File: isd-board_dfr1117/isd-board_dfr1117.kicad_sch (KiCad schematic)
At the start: 50 parts, among them J1 BATT, J10 Conn_01x13, J2 Conn_01x08, J3 Conn_01x02_Pin, J4 Conn_01x08, J5 Conn_01x04, J6 Conn_01x04, J7 Conn_01x05, J8 USB_C_Receptacle_PowerOnly_6P, J9 Conn_01x02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

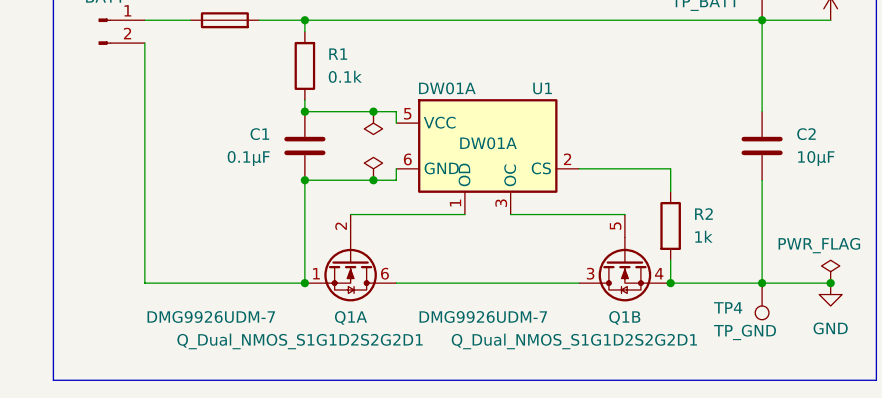
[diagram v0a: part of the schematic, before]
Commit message: update: battery protection circuit (compact placement)
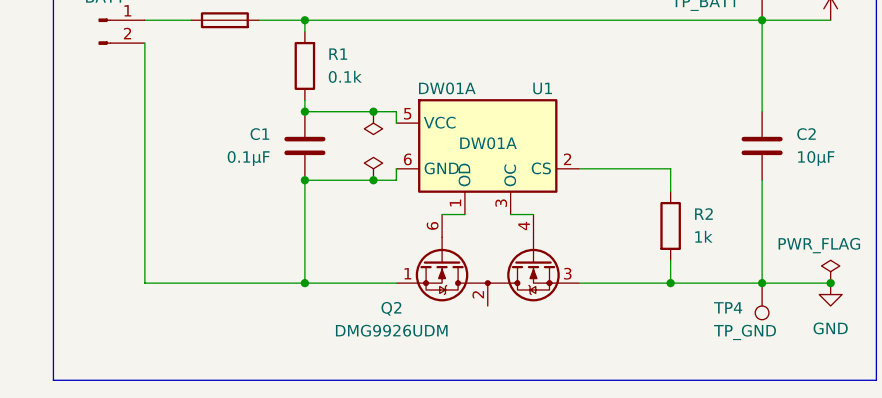
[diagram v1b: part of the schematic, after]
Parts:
- removed Q1: Q_Dual_NMOS_S1G1D2S2G2D1, Package_TO_SOT_SMD:SOT-23-6_Handsoldering, symbol Transistor_FET:Q_Dual_NMOS_S1G1D2S2G2D1
- added Q2: DMG9926UDM, Package_TO_SOT_SMD:SOT-23-6, symbol Transistor_FET:DMG9926UDM
- TP2, TP3, TP4, TP5, TP6, TP7: footprint TestPoint:TestPoint_Pad_D2.5mm -> TestPoint:TestPoint_Pad_D1.0mm
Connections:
- net GND: now also Q2.3 (S2)
- net at U1.1 (OD): now also Q2.6 (G1)
- net at U1.3 (OC): now also Q2.4 (G2)
- net at C1.2, J1.2 (Pin_2), U1.6 (GND): now also Q2.1 (D1)
- new net: Q2.2 (S1/D2), Q2.5 (S1/D2)
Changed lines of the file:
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@@
 	)
 	(junction
-		(at 46.99 181.61)
+		(at 87.63 181.61)
 		(diameter 0)
 		(color 0 0 0 0)
@@
 	)
 	(junction
-		(at 87.63 181.61)
-		(diameter 0)
-		(color 0 0 0 0)
-	)
-	(junction
 		(at 57.15 101.6)
 		(diameter 0)
@@
 	)
 	(junction
+		(at 46.99 181.61)
+		(diameter 0)
+		(color 0 0 0 0)
+	)
+	(junction
 		(at 54.61 162.56)
 		(diameter 0)
@@
 	(wire
 		(pts
-			(xy 57.15 181.61) (xy 77.47 181.61)
+			(xy 242.57 77.47) (xy 245.11 77.47)
 		)
 		(stroke
@@
 	(wire
 		(pts
-			(xy 242.57 77.47) (xy 245.11 77.47)
+			(xy 97.79 152.4) (xy 97.79 162.56)
 		)
 		(stroke
@@
 	(wire
 		(pts
-			(xy 97.79 152.4) (xy 97.79 162.56)
+			(xy 57.15 101.6) (xy 57.15 102.87)
 		)
 		(stroke
@@
 	(wire
 		(pts
-			(xy 57.15 101.6) (xy 57.15 102.87)
+			(xy 189.23 156.21) (xy 199.39 156.21)
 		)
 		(stroke
@@
 	(wire
 		(pts
-			(xy 189.23 156.21) (xy 199.39 156.21)
+			(xy 29.21 154.94) (xy 29.21 181.61)
 		)
 		(stroke
@@
 	(wire
 		(pts
-			(xy 29.21 154.94) (xy 29.21 181.61)
+			(xy 46.99 170.18) (xy 46.99 181.61)
 		)
 		(stroke
@@
 	(wire
 		(pts
-			(xy 46.99 170.18) (xy 46.99 181.61)
+			(xy 77.47 181.61) (xy 87.63 181.61)
 		)
 		(stroke
@@
 	(wire
 		(pts
+			(xy 62.23 173.99) (xy 64.77 173.99)
+		)
+		(stroke
+			(width 0)
+			(type default)
+		)
+	)
+	(wire
+		(pts
 			(xy 30.48 91.44) (xy 30.48 92.71)
 		)
@@
 	(wire
 		(pts
-			(xy 69.85 173.99) (xy 82.55 173.99)
+			(xy 129.54 181.61) (xy 133.35 181.61)
 		)
 		(stroke
@@
 	(wire
 		(pts
-			(xy 129.54 181.61) (xy 133.35 181.61)
+			(xy 167.64 168.91) (xy 162.56 168.91)
 		)
 		(stroke
@@
 	(wire
 		(pts
-			(xy 167.64 168.91) (xy 162.56 168.91)
+			(xy 46.99 181.61) (xy 57.15 181.61)
 		)
 		(stroke
@@
 	(wire
 		(pts
+			(xy 69.85 173.99) (xy 72.39 173.99)
+		)
+		(stroke
+			(width 0)
+			(type default)
+		)
+	)
+	(wire
+		(pts
 			(xy 29.21 152.4) (xy 34.29 152.4)
 		)
@@
 	(wire
 		(pts
-			(xy 52.07 173.99) (xy 64.77 173.99)
-		)
-		(stroke
-			(width 0)
-			(type default)
-		)
-	)
-	(wire
-		(pts
 			(xy 71.12 120.65) (xy 77.47 120.65)
 		)
@@
 			)
 		)
-		(property "Footprint" "TestPoint:TestPoint_Pad_D2.5mm"
+		(property "Footprint" "TestPoint:TestPoint_Pad_D1.0mm"
 			(at 160.02 161.29 0)
 			(effects
@@
 			)
 		)
-		(property "Footprint" "TestPoint:TestPoint_Pad_D2.5mm"
+		(property "Footprint" "TestPoint:TestPoint_Pad_D1.0mm"
 			(at 220.98 120.65 0)
 			(effects
@@
 			)
 		)
-		(property "Footprint" "TestPoint:TestPoint_Pad_D2.5mm"
+		(property "Footprint" "TestPoint:TestPoint_Pad_D1.0mm"
 			(at 92.71 181.61 0)
 			(effects
@@
 			)
 		)
-		(property "Footprint" "TestPoint:TestPoint_Pad_D2.5mm"
+		(property "Footprint" "TestPoint:TestPoint_Pad_D1.0mm"
 			(at 80.01 91.44 0)
 			(effects
@@
 	)
 	(symbol
-		(lib_id "Transistor_FET:Q_Dual_NMOS_S1G1D2S2G2D1")
-		(at 52.07 179.07 270)
-		(unit 1)
-		(exclude_from_sim no)
-		(in_bom yes)
-		(on_board yes)
-		(dnp no)
-		(property "Reference" "Q1"
-			(at 52.07 185.42 90)
-			(effects
-				(font
-					(size 1.27 1.27)
-				)
-			)
-		)
-		(property "Value" "Q_Dual_NMOS_S1G1D2S2G2D1"
-			(at 46.482 187.96 90)
-			(effects
-				(font
-					(size 1.27 1.27)
-				)
-			)
-		)
-		(property "Footprint" "Package_TO_SOT_SMD:SOT-23-6_Handsoldering"
-			(at 52.07 184.15 0)
-			(effects
-				(font
-					(size 1.27 1.27)
-				)
-				(hide yes)
-			)
-		)
-		(property "Datasheet" "https://www.mouser.fi/datasheet/3/175/1/ds31770.pdf"
-			(at 52.07 184.15 0)
-			(effects
-				(font
-					(size 1.27 1.27)
-				)
-				(hide yes)
-			)
-		)
-		(property "Description" "Dual NMOS transistor, 6 pin package"
-			(at 52.07 179.07 0)
-			(effects
-				(font
-					(size 1.27 1.27)
-				)
-				(hide yes)
-			)
-		)
-		(property "MPN" "DMG9926UDM-7"
-			(at 36.576 185.42 90)
-			(effects
-				(font
-					(size 1.27 1.27)
-				)
-			)
-		)
-		(pin "1"
-		)
-		(pin "6"
-		)
-		(pin "4"
-		)
-		(pin "2"
-		)
-		(pin "5"
-		)
-		(pin "3"
-		)
-		(instances
-			(project ""
-				(path "/27bbddde-1315-4a7b-91f8-52269d45b0e3"
-					(reference "Q1")
-					(unit 1)
-				)
-			)
-		)
-	)
-	(symbol
 		(lib_id "Device:C")
 		(at 97.79 166.37 0)
@@
 	)
 	(symbol
-		(lib_id "Transistor_FET:Q_Dual_NMOS_S1G1D2S2G2D1")
-		(at 82.55 179.07 90)
-		(mirror x)
-		(unit 2)
-		(exclude_from_sim no)
-		(in_bom yes)
-		(on_board yes)
-		(dnp no)
-		(property "Reference" "Q1"
-			(at 82.55 185.42 90)
-			(effects
-				(font
-					(size 1.27 1.27)
-				)
-			)
-		)
-		(property "Value" "Q_Dual_NMOS_S1G1D2S2G2D1"
-			(at 76.962 187.96 90)
-			(effects
-				(font
-					(size 1.27 1.27)
-				)
-			)
-		)
-		(property "Footprint" "Package_TO_SOT_SMD:SOT-23-6_Handsoldering"
-			(at 82.55 184.15 0)
-			(effects
-				(font
-					(size 1.27 1.27)
-				)
-				(hide yes)
-			)
-		)
-		(property "Datasheet" "https://www.mouser.fi/datasheet/3/175/1/ds31770.pdf"
-			(at 82.55 184.15 0)
-			(effects
-				(font
-					(size 1.27 1.27)
-				)
-				(hide yes)
-			)
-		)
-		(property "Description" "Dual NMOS transistor, 6 pin package"
-			(at 82.55 179.07 0)
-			(effects
-				(font
-					(size 1.27 1.27)
-				)
-				(hide yes)
-			)
-		)
-		(property "MPN" "DMG9926UDM-7"
-			(at 66.802 185.42 90)
-			(effects
-				(font
-					(size 1.27 1.27)
-				)
-			)
-		)
-		(pin "1"
-		)
-		(pin "6"
-		)
-		(pin "4"
-		)
-		(pin "2"
-		)
-		(pin "5"
-		)
-		(pin "3"
-		)
-		(instances
-			(project ""
-				(path "/27bbddde-1315-4a7b-91f8-52269d45b0e3"
-					(reference "Q1")
-					(unit 2)
-				)
-			)
-		)
-	)
-	(symbol
 		(lib_id "power:GND")
 		(at 133.35 184.15 0)
@@
 	)
 	(symbol
+		(lib_id "Transistor_FET:DMG9926UDM")
+		(at 67.31 181.61 90)
+		(mirror x)
+		(unit 1)
+		(exclude_from_sim no)
+		(in_bom yes)
+		(on_board yes)
+		(dnp no)
+		(property "Reference" "Q2"
+			(at 56.642 184.404 90)
+			(effects
+				(font
+					(size 1.27 1.27)
+				)
+			)
+		)
+		(property "Value" "DMG9926UDM"
+			(at 56.642 186.944 90)
+			(effects
+				(font
+					(size 1.27 1.27)
+				)
+			)
+		)
+		(property "Footprint" "Package_TO_SOT_SMD:SOT-23-6"
+			(at 71.12 184.15 0)
+			(effects
+				(font
+					(size 1.27 1.27)
+					(italic yes)
+				)
+				(justify left)
+				(hide yes)
+			)
+		)
+		(property "Datasheet" "https://www.diodes.com/assets/Datasheets/ds31770.pdf"
+			(at 73.025 184.15 0)
+			(effects
+				(font
+					(size 1.27 1.27)
+				)
+				(justify left)
+				(hide yes)
+			)
+		)
+		(property "Description" "4.2A Id, 20V Vds, Common-Drain, Dual Half Bridge N-Channel MOSFET, 28mOhm Ron, SOT-23-6"
+			(at 67.31 181.61 0)
+			(effects
+				(font
+					(size 1.27 1.27)
+				)
+				(hide yes)
+			)
+		)
+		(pin "2"
+		)
+		(pin "5"
+		)
+		(pin "6"
+		)
+		(pin "3"
+		)
+		(pin "1"
+		)
+		(pin "4"
+		)
+		(instances
+			(project ""
+				(path "/27bbddde-1315-4a7b-91f8-52269d45b0e3"
+					(reference "Q2")
+					(unit 1)
+				)
+			)
+		)
+	)
+	(symbol
 		(lib_id "Connector:TestPoint")
 		(at 157.48 83.82 270)
@@
 			)
 		)
-		(property "Footprint" "TestPoint:TestPoint_Pad_D2.5mm"
+		(property "Footprint" "TestPoint:TestPoint_Pad_D1.0mm"
 			(at 157.48 88.9 0)
 			(effects
@@
 			)
 		)
-		(property "Footprint" "TestPoint:TestPoint_Pad_D2.5mm"
+		(property "Footprint" "TestPoint:TestPoint_Pad_D1.0mm"
 			(at 92.71 152.4 0)
 			(effects
